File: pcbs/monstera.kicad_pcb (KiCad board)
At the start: 2 copper layers, 12 parts, among them J1 Conn_01x04_Socket, J2 Conn_01x04_Socket, J3 Conn_01x04_Socket, J4 Conn_01x03_Socket, J5 Conn_01x03_Socket, J6 Conn_01x03_Socket, U1 ESP32-S3 Supermini, U2 LD2450, U3 ER_OLEDM0.91_1x-I2C, U4 LD2410C

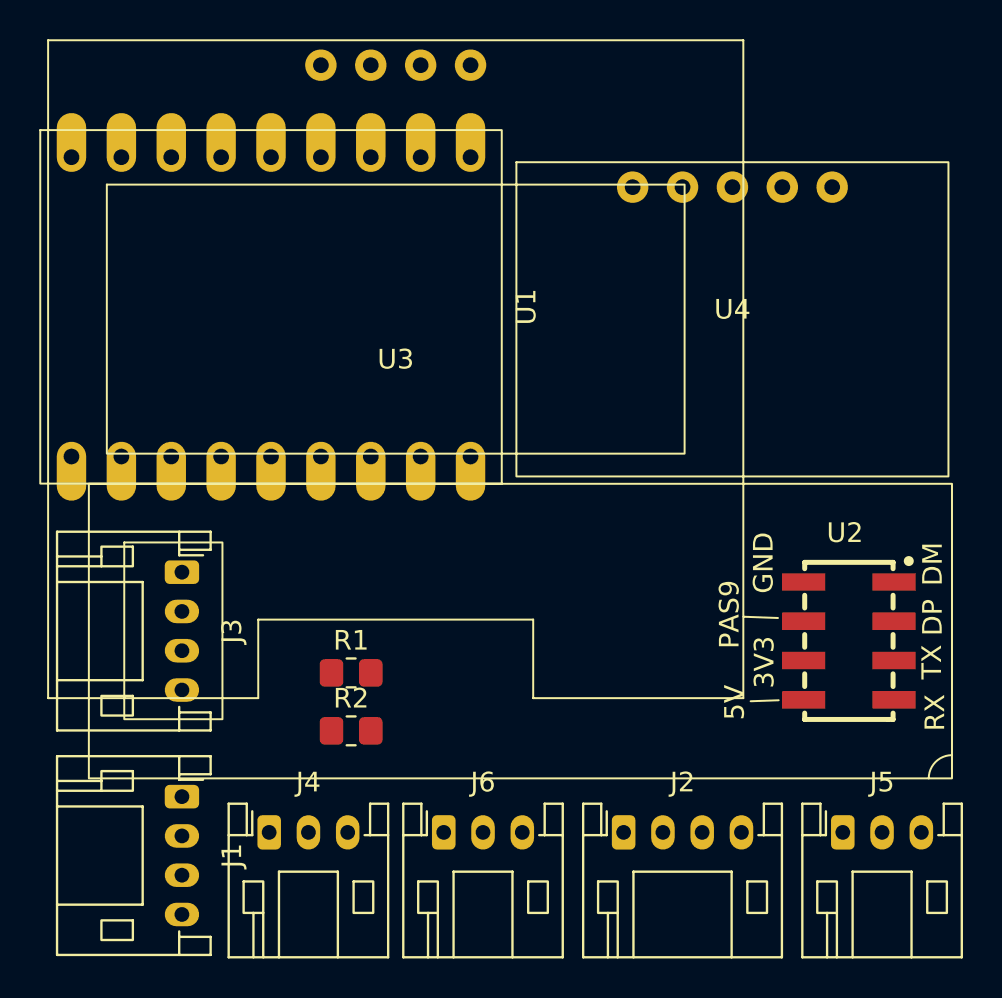
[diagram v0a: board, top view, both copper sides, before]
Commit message: pcb: remove OLED display
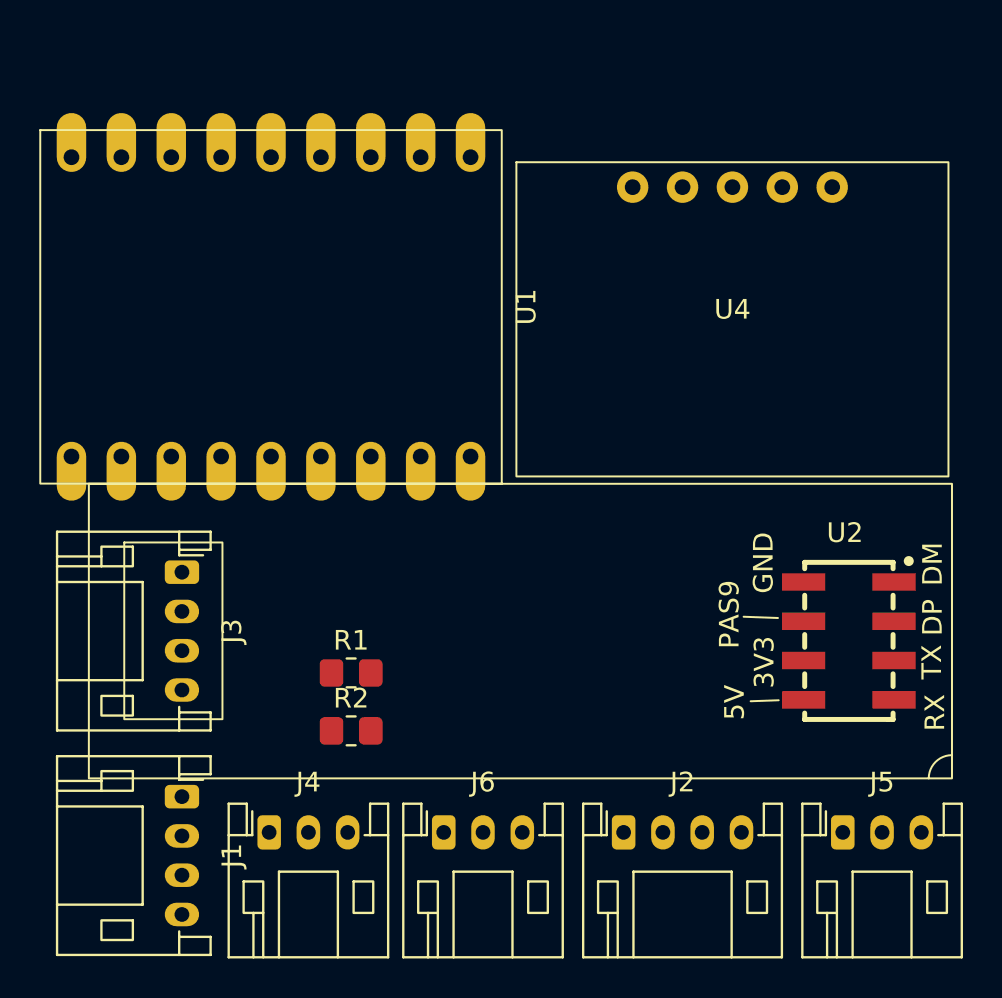
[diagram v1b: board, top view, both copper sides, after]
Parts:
- removed U3: ER_OLEDM0.91_1x-I2C, Aloe:SSD1306_1.3
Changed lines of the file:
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@@
 		)
-	)
-	(footprint "Aloe:SSD1306_1.3"
-		(layer "F.Cu")
-		(at 82.55 52.705)
-		(property "Reference" "U3"
-			(at 0 -0.5 0)
-			(unlocked yes)
-			(layer "F.SilkS")
-			(effects
-				(font
-					(size 1 1)
-					(thickness 0.1)
-				)
-			)
-		)
-		(property "Value" "ER_OLEDM0.91_1x-I2C"
-			(at 0 1 0)
-			(unlocked yes)
-			(layer "F.Fab")
-			(effects
-				(font
-					(size 1 1)
-					(thickness 0.15)
-				)
-			)
-		)
-		(property "Datasheet" "https://www.buydisplay.com/download/manual/ER-OLEDM0.91-1_Datasheet.pdf"
-			(at 0 0 0)
-			(unlocked yes)
-			(layer "F.Fab")
-			(hide yes)
-			(effects
-				(font
-					(size 1 1)
-					(thickness 0.15)
-				)
-			)
-		)
-		(property "Description" "SSD1306 OLED module, 0.91 inch, 128x32, I2C"
-			(at 0 0 0)
-			(unlocked yes)
-			(layer "F.Fab")
-			(hide yes)
-			(effects
-				(font
-					(size 1 1)
-					(thickness 0.15)
-				)
-			)
-		)
-		(property ki_fp_filters "ER?OLEDM0.91?1x?I2C*")
-		(sheetname "/")
-		(sheetfile "monstera.kicad_sch")
-		(units
-			(unit
-				(name "A")
-				(pins "3" "4" "2" "1")
-			)
-		)
-		(attr smd)
-		(duplicate_pad_numbers_are_jumpers no)
-		(fp_line
-			(start -17.7 -16.75)
-			(end 17.7 -16.75)
-			(stroke
-				(width 0.1)
-				(type default)
-			)
-			(layer "F.SilkS")
-		)
-		(fp_line
-			(start -17.7 16.75)
-			(end -17.7 -16.75)
-			(stroke
-				(width 0.1)
-				(type default)
-			)
-			(layer "F.SilkS")
-		)
-		(fp_line
-			(start -17.7 16.75)
-			(end -7 16.75)
-			(stroke
-				(width 0.1)
-				(type default)
-			)
-			(layer "F.SilkS")
-		)
-		(fp_line
-			(start -7 12.75)
-			(end 7 12.75)
-			(stroke
-				(width 0.1)
-				(type default)
-			)
-			(layer "F.SilkS")
-		)
-		(fp_line
-			(start -7 16.75)
-			(end -7 12.75)
-			(stroke
-				(width 0.1)
-				(type solid)
-			)
-			(layer "F.SilkS")
-		)
-		(fp_line
-			(start 7 16.75)
-			(end 7 12.75)
-			(stroke
-				(width 0.1)
-				(type solid)
-			)
-			(layer "F.SilkS")
-		)
-		(fp_line
-			(start 17.7 -16.75)
-			(end 17.7 16.75)
-			(stroke
-				(width 0.1)
-				(type default)
-			)
-			(layer "F.SilkS")
-		)
-		(fp_line
-			(start 17.7 16.75)
-			(end 7 16.75)
-			(stroke
-				(width 0.1)
-				(type solid)
-			)
-			(layer "F.SilkS")
-		)
-		(fp_rect
-			(start -14.71 -9.4)
-			(end 14.71 4.3)
-			(stroke
-				(width 0.1)
-				(type default)
-			)
-			(fill no)
-			(layer "F.SilkS")
-		)
-		(fp_rect
-			(start -17.5 -11.36)
-			(end 17.5 11.64)
-			(stroke
-				(width 0.1)
-				(type default)
-			)
-			(fill no)
-			(layer "User.1")
-		)
-		(fp_text user "${REFERENCE}"
-			(at 0 2.5 0)
-			(unlocked yes)
-			(layer "F.Fab")
-			(effects
-				(font
-					(size 1 1)
-					(thickness 0.15)
-				)
-			)
-		)
-		(pad "1" thru_hole circle
-			(at -3.81 -15.48)
-			(size 1.6 1.6)
-			(drill 0.8)
-			(layers "*.Cu" "*.Mask")
-			(remove_unused_layers no)
-			(net "GND")
-			(pinfunction "GND_1")
-			(pintype "power_in")
-		)
-		(pad "2" thru_hole circle
-			(at -1.27 -15.48)
-			(size 1.6 1.6)
-			(drill 0.8)
-			(layers "*.Cu" "*.Mask")
-			(remove_unused_layers no)
-			(net "+3V3")
-			(pinfunction "VCC_2")
-			(pintype "power_in")
-		)
-		(pad "3" thru_hole circle
-			(at 1.27 -15.48)
-			(size 1.6 1.6)
-			(drill 0.8)
-			(layers "*.Cu" "*.Mask")
-			(remove_unused_layers no)
-			(net "/I2CSCL")
-			(pinfunction "SCL_3")
-			(pintype "input")
-		)
-		(pad "4" thru_hole circle
-			(at 3.81 -15.48)
-			(size 1.6 1.6)
-			(drill 0.8)
-			(layers "*.Cu" "*.Mask")
-			(remove_unused_layers no)
-			(net "/I2CSDA")
-			(pinfunction "SDA_4")
-			(pintype "bidirectional")
-		)
-		(embedded_fonts no)
 	)
 	(footprint "Connector_JST:JST_PH_S3B-PH-K_1x03_P2.00mm_Horizontal"

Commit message: make sensor pcbs
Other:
- board text added: "might change to different footprint with tht holes will likely need to desolder JST connector to avoid interference or confusion"
- board text removed: "might change to different footprint with tht holes"
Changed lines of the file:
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@@
 		(embedded_fonts no)
 	)
-	(gr_text "might change to different footprint with tht holes\n"
+	(gr_text "might change to different footprint with tht holes\nwill likely need to desolder JST connector to avoid interference or confusion"
 		(at 111.125 65.405 0)
 		(layer "User.4")
